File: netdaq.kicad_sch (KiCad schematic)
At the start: 0 parts

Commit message: did stuff
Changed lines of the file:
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@@
 	)
 	(label "MCU_SPI3_ADC2{SPI}"
-		(at 210.82 151.13 90)
+		(at 210.3974 151.1476 90)
 		(effects
 			(font
@@
 			)
 		)
-		(pin "SPI3{SPI}" bidirectional
-			(at 210.82 130.81 270)
-			(effects
-				(font
-					(size 1.27 1.27)
-				)
-				(justify left)
-			)
-		)
-		(pin "SPI5{SPI}" bidirectional
-			(at 213.36 130.81 270)
-			(effects
-				(font
-					(size 1.27 1.27)
-				)
-				(justify left)
-			)
-		)
-		(pin "SPI6{SPI}" bidirectional
-			(at 215.9 130.81 270)
-			(effects
-				(font
-					(size 1.27 1.27)
-				)
-				(justify left)
-			)
-		)
 		(pin "{JTAG}" bidirectional
 			(at 232.41 118.11 0)
@@
 			(effects
 				(font
+					(size 1.27 1.27)
+				)
+				(justify left)
+			)
+		)
+		(pin "SPI3{SPI}" bidirectional
+			(at 215.9 130.81 270)
+			(effects
+				(font
+					(size 1.27 1.27)
+				)
+				(justify left)
+			)
+		)
+		(pin "SPI5{SPI}" bidirectional
+			(at 210.82 130.81 270)
+			(effects
+				(font
+					(size 1.27 1.27)
+				)
+				(justify left)
+			)
+		)
+		(pin "SPI6{SPI}" bidirectional
+			(at 213.36 130.81 270)
+			(effects
+				(font

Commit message: stuff
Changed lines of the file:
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@@
+	(bus
+		(pts
+			(xy 213.36 45.72) (xy 213.36 97.79)
+		)
+		(stroke
+			(width 0)
+			(type default)
+		)
+	)
 	(bus
 		(pts
@@
 		(pts
 			(xy 215.9 45.72) (xy 215.9 97.79)
-		)
-		(stroke
-			(width 0)
-			(type default)
-		)
-	)
-	(bus
-		(pts
-			(xy 213.36 45.72) (xy 213.36 97.79)
 		)
 		(stroke
@@
 		)
 	)
-	(label "RMII{RMII}"
-		(at 213.36 73.66 90)
-		(effects
-			(font
-				(size 1.27 1.27)
-			)
-			(justify left bottom)
-		)
-	)
 	(label "MCU_ETH_RST#"
 		(at 210.82 73.66 90)
@@
 		)
 	)
+	(label "RMII{RMII}"
+		(at 213.36 97.79 90)
+		(effects
+			(font
+				(size 1.27 1.27)
+			)
+			(justify left bottom)
+		)
+	)
 	(label "MCU_SPI3_ADC2{SPI}"
-		(at 210.3974 151.1476 90)
-		(effects
-			(font
+		(at 210.82 151.13 90)
+		(effects
+			(font

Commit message: lots
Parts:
- added H1, H2, H3, H4: MountingHole, MountingHole:MountingHole_3.2mm_M3_ISO14580, symbol Mechanical:MountingHole
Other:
- sheet PD Controller ports: added POE_V+, VIN+, VIN-; removed none
- sheet PoE Regulator ports: added VIN; removed none

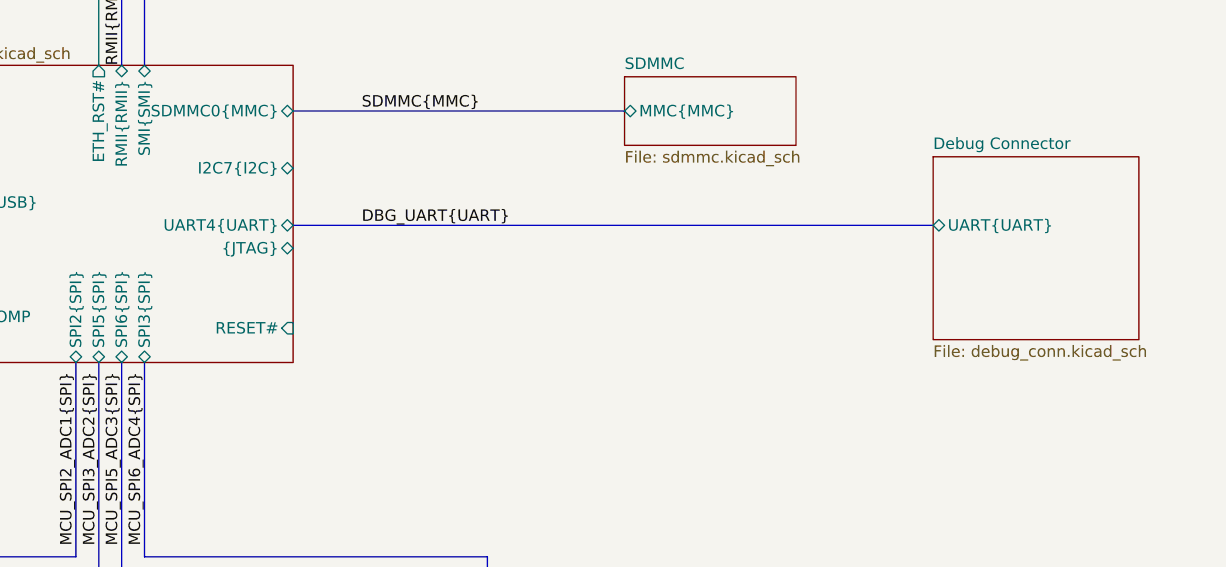
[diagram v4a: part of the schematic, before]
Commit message: changed to 4 layer, finished usb conn, added jtag conn, some other things
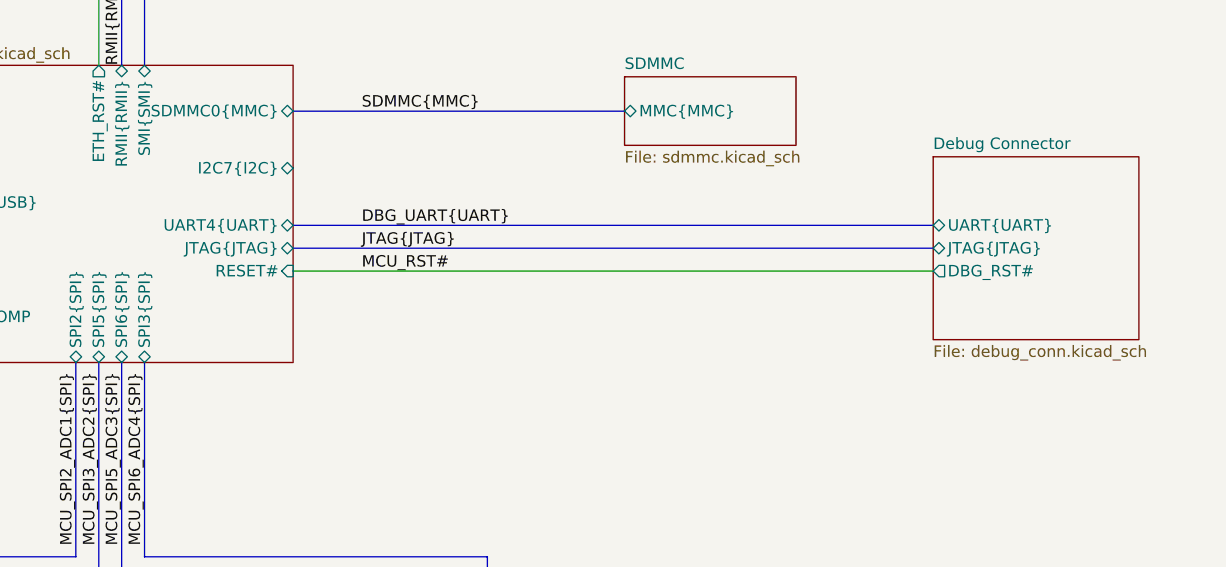
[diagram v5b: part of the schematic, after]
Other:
- sheet Debug Connector ports: added DBG_RST#, JTAG{JTAG}; removed none
- sheet MCU ports: added JTAG{JTAG}; removed {JTAG}
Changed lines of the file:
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@@
+		)
+	)
+	(bus
+		(pts
+			(xy 232.41 118.11) (xy 303.53 118.11)
+		)
+		(stroke
+			(width 0)
+			(type default)
 		)
 	)
@@
 		(pts
 			(xy 170.18 215.9) (xy 170.18 236.22)
+		)
+		(stroke
+			(width 0)
+			(type default)
+		)
+	)
+	(wire
+		(pts
+			(xy 232.41 120.65) (xy 303.53 120.65)
 		)
 		(stroke
@@
 		)
 	)
+	(label "MCU_RST#"
+		(at 240.03 120.65 0)
+		(effects
+			(font
+				(size 1.27 1.27)
+			)
+			(justify left bottom)
+		)
+	)
 	(label "USB{USB}"
 		(at 180.34 113.03 0)
@@
 		)
 	)
+	(label "JTAG{JTAG}"
+		(at 240.03 118.11 0)
+		(effects
+			(font
+				(size 1.27 1.27)
+			)
+			(justify left bottom)
+		)
+	)
 	(label "GPIO[17..24]"
 		(at 226.06 228.6 90)
@@
 			)
 		)
+		(pin "DBG_RST#" output
+			(at 303.53 120.65 180)
+			(effects
+				(font
+					(size 1.27 1.27)
+				)
+				(justify left)
+			)
+		)
+		(pin "JTAG{JTAG}" bidirectional
+			(at 303.53 118.11 180)
+			(effects
+				(font
+					(size 1.27 1.27)
+				)
+				(justify left)
+			)
+		)
 		(instances
 			(project "netdaq"
@@
 			)
 		)
-		(pin "{JTAG}" bidirectional
-			(at 232.41 118.11 0)
-			(effects
-				(font
-					(size 1.27 1.27)
-				)
-				(justify right)
-			)
-		)
 		(pin "RESET#" input
-			(at 232.41 127 0)
+			(at 232.41 120.65 0)
 			(effects
 				(font
@@
 			)
 		)
+		(pin "JTAG{JTAG}" bidirectional
+			(at 232.41 118.11 0)
+			(effects
+				(font
+					(size 1.27 1.27)
+				)
+				(justify right)
+			)
+		)

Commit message: did almost nothing!
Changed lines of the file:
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@@
 	)
 	(sheet
-		(at 133.35 85.09)
+		(at 132.08 82.55)
 		(size 19.05 17.78)
 		(exclude_from_sim no)
@@
 		)
 		(property "Sheetname" "3V3 Regulator"
-			(at 133.35 84.3784 0)
+			(at 132.08 81.8384 0)
 			(show_name no)
 			(do_not_autoplace no)
@@
 		)
 		(property "Sheetfile" "3v3_reg.kicad_sch"
-			(at 133.35 103.4546 0)
+			(at 132.08 100.9146 0)
 			(show_name no)
 			(do_not_autoplace no)

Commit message: bunch of stuff
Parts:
- H1, H2, H3, H4: now not fitted
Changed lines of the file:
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@@
 		(on_board yes)
 		(in_pos_files yes)
-		(dnp no)
+		(dnp yes)
 		(fields_autoplaced yes)
 		(property "Reference" "H3"
@@
 		(on_board yes)
 		(in_pos_files yes)
-		(dnp no)
+		(dnp yes)
 		(fields_autoplaced yes)
 		(property "Reference" "H2"
@@
 		(on_board yes)
 		(in_pos_files yes)
-		(dnp no)
+		(dnp yes)
 		(fields_autoplaced yes)
 		(property "Reference" "H1"
@@
 		(on_board yes)
 		(in_pos_files yes)
-		(dnp no)
+		(dnp yes)
 		(fields_autoplaced yes)
 		(property "Reference" "H4"
